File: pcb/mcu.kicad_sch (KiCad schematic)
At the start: 35 parts, among them J1 XF2M-1415-1A, SW1 EVQ-Q2B02W, SW2 EVQ-Q2B02W, U1 ESP32-S3-WROOM-1-N8R2

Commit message: Clean up and consistency
Moved buzzer to MCU
Fixed model directory
Set font size
Set outline size
Upscaled Roxy ❤️
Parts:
- added C10: 1uF, CRGM Passive:C_0603_1608Metric, symbol Device:C
- added D2: D_Schottky, CRGM Passive:D_SOD-523, symbol Device:D_Schottky
- added LS1: FUET-5025, CRG Makes:FUET-5025, symbol CRG Makes:CMT-0502-75-SMT-TR
- added Q1: MMBT2222A, CRGM Passive:SOT-523, symbol Transistor_BJT:MMBT2222A
- added R12: 1K, CRGM Passive:R_0603_1608Metric, symbol Device:R_US
- added TP42: ~, CRGM Mechanical:TestPoint_Pad_D1.0mm, symbol Connector:TestPoint
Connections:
- net +3.3V: now also C10.1, D2.1 (K), LS1.2 (+)
- net BUZZER: now also R12.1, TP42.1
- net GND: now also C10.2, Q1.2 (E)
- new net: Q1.1 (B), R12.2
- new net BUZZ_GND: D2.2 (A), LS1.3 (-), Q1.3 (C)
- no-connect marks 5 -> 6
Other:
- note added: "Buzzer"
- note added: "On Board LED"
- note removed: "ON BOARD LED"
- moved on the sheet: C7, D1, J1, TP13, TP14, TP15, TP16, TP17, TP18, TP19, TP20, TP21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

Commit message: Updated part attributes for consistency.
Updated requirements section to be more accurate.
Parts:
- C1, C10, C2, C4, C5, C7: Tolerance (none) -> 10%
- R1, R12, R2, R3: Tolerance (none) -> 5%
- U1: MN (none) -> Espressif; MPN (none) -> ESP32-S3-WROOM-1-N8R2
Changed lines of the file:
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@@
 			)
 		)
+		(property "Tolerance" "5%"
+			(at 81.28 109.22 0)
+			(effects
+				(font
+					(size 1.27 1.27)
+				)
+				(hide yes)
+			)
+		)
 		(pin "2"
 		)
@@
 			)
 		)
+		(property "Tolerance" "10%"
+			(at 39.37 162.56 0)
+			(effects
+				(font
+					(size 1.27 1.27)
+				)
+				(hide yes)
+			)
+		)
 		(pin "2"
 		)
@@
 			)
 		)
+		(property "Tolerance" "5%"
+			(at 157.48 102.87 90)
+			(effects
+				(font
+					(size 1.27 1.27)
+				)
+				(hide yes)
+			)
+		)
 		(pin "2"
 		)
@@
 			)
 		)
+		(property "Tolerance" "5%"
+			(at 90.17 109.22 0)
+			(effects
+				(font
+					(size 1.27 1.27)
+				)
+				(hide yes)
+			)
+		)
 		(pin "2"
 		)
@@
 			)
 		)
+		(property "Tolerance" "5%"
+			(at 30.48 144.78 0)
+			(effects
+				(font
+					(size 1.27 1.27)
+				)
+				(hide yes)
+			)
+		)
 		(pin "2"
 		)
@@
 			)
 		)
+		(property "Tolerance" "10%"
+			(at 123.19 114.3 0)
+			(effects
+				(font
+					(size 1.27 1.27)
+				)
+				(hide yes)
+			)
+		)
 		(pin "2"
 		)
@@
 			)
 		)
+		(property "Tolerance" "10%"
+			(at 87.63 161.29 0)
+			(effects
+				(font
+					(size 1.27 1.27)
+				)
+				(hide yes)
+			)
+		)
 		(pin "1"
 		)
@@
 			)
 		)
+		(property "Tolerance" "10%"
+			(at 198.12 109.22 0)
+			(effects
+				(font
+					(size 1.27 1.27)
+				)
+				(hide yes)
+			)
+		)
 		(pin "1"
 		)
@@
 			)
 		)
+		(property "Tolerance" "10%"
+			(at 111.76 114.3 0)
+			(effects
+				(font
+					(size 1.27 1.27)
+				)
+				(hide yes)
+			)
+		)
 		(pin "1"
 		)
@@
 			)
 		)
+		(property "MN" "Espressif"
+			(at 73.66 58.42 0)
+			(effects
+				(font
+					(size 1.27 1.27)
+				)
+				(hide yes)
+			)
+		)
+		(property "MPN" "ESP32-S3-WROOM-1-N8R2"
+			(at 73.66 58.42 0)
+			(effects
+				(font
+					(size 1.27 1.27)
+				)
+				(hide yes)
+			)
+		)
 		(pin "5"
 		)
@@
 			(at 251.46 109.22 0)
 			(effects
+				(font
+					(size 1.27 1.27)
+				)
+				(hide yes)
+			)
+		)
+		(property "Tolerance" "10%"
+			(at 251.46 109.22 0)
+			(effects

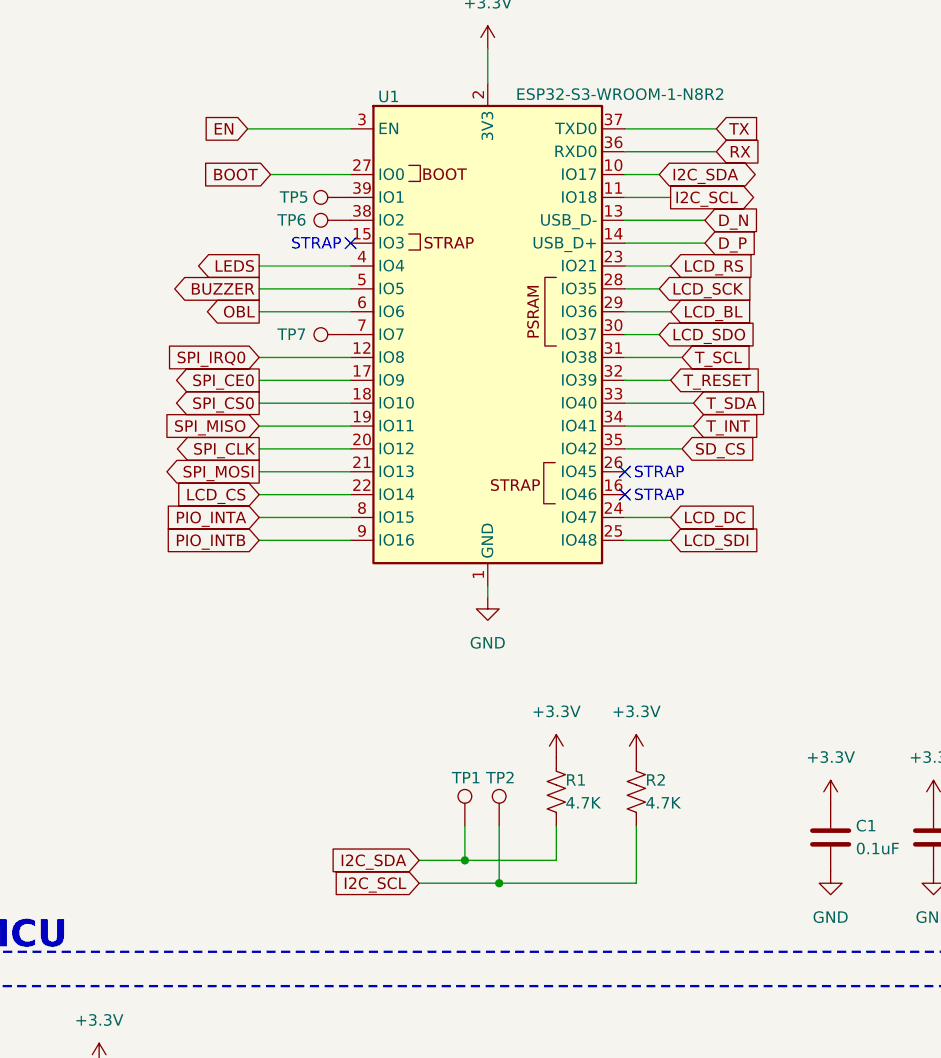
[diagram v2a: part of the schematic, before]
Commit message: Switched to internal and external I2C bus
Updated renders
Updated description of QWICC connectors
Added test points for INT I2C
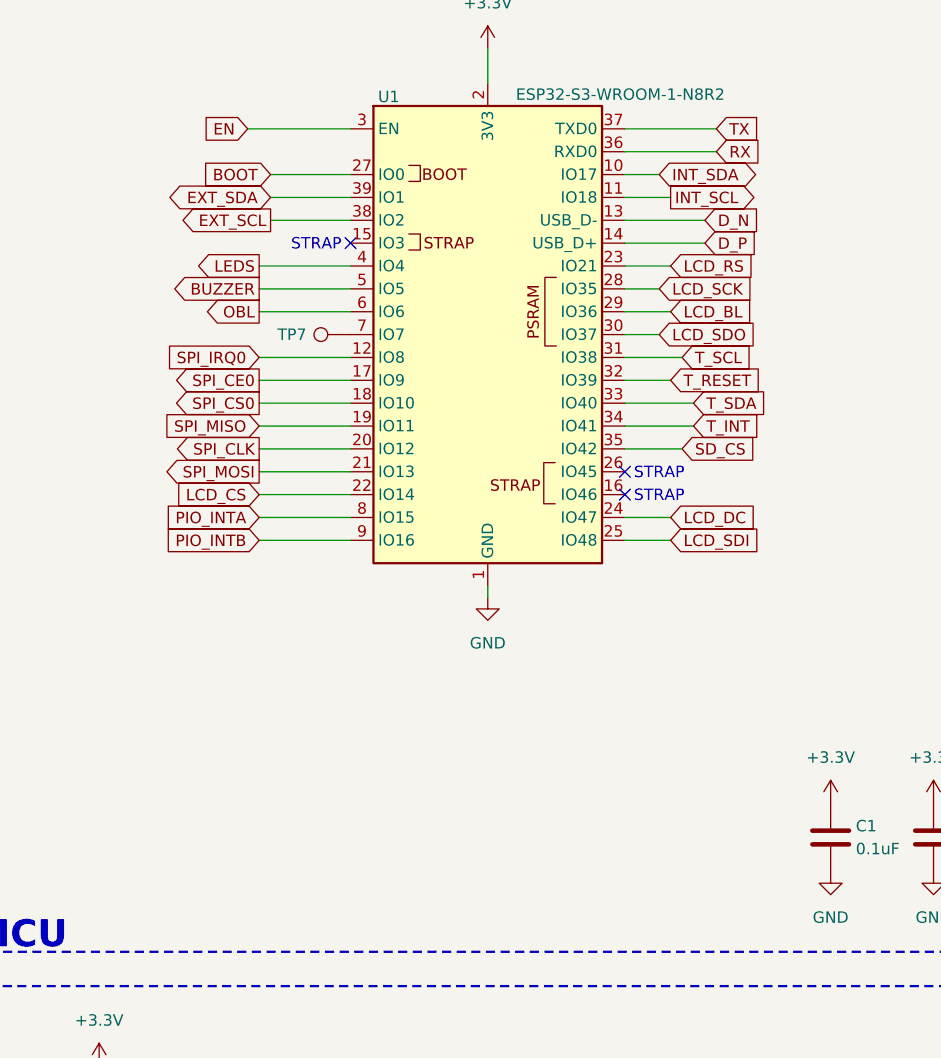
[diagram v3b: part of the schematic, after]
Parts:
- removed R1, R2: 4.7K, CRGM Passive:R_0603_1608Metric, symbol Device:R_US
- removed TP1, TP2, TP5, TP6: ~, CRGM Mechanical:TestPoint_Pad_D1.0mm, symbol Connector:TestPoint
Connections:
- net EXT_SDA: now reaches U1.39 (IO1)
- net EXT_SCL: now reaches U1.38 (IO2)
- net I2C_SCL renamed INT_SCL
- net I2C_SDA renamed INT_SDA

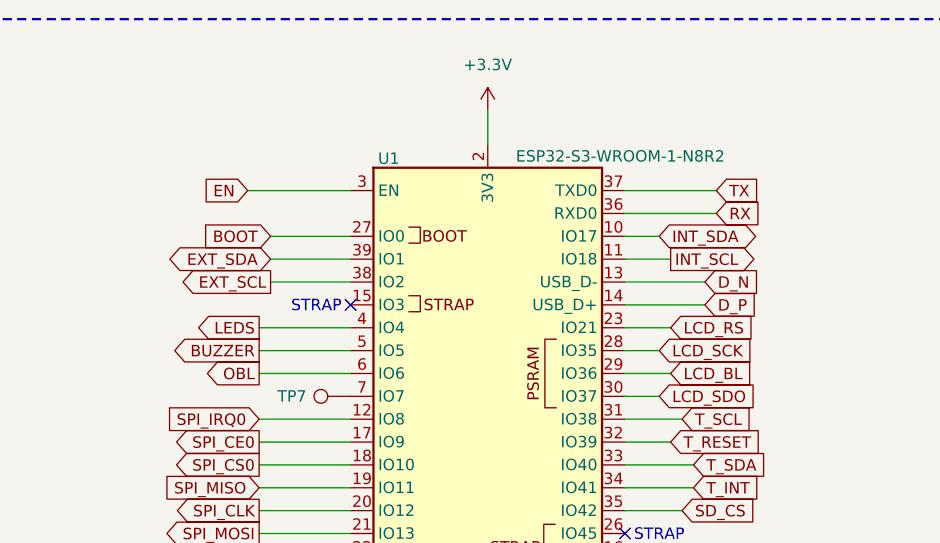
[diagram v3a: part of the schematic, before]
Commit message: Rework to add power connector
Simplified GPIO connectors to make sure for power.
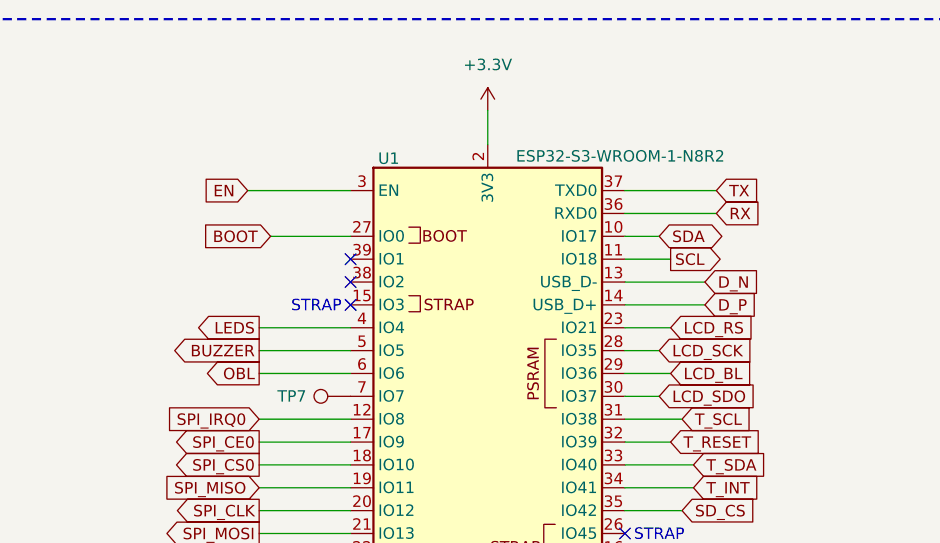
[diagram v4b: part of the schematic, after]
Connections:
- net EXT_SCL: no longer names the net of U1.38 (IO2)
- net EXT_SDA: no longer names the net of U1.39 (IO1)
- net INT_SCL renamed SCL
- net INT_SDA renamed SDA
- no-connect marks 6 -> 8
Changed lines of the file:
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@@
 	)
 	(no_connect
+		(at 58.42 45.72)
+	)
+	(no_connect
 		(at 171.45 87.63)
 	)
 	(no_connect
+		(at 58.42 43.18)
+	)
+	(no_connect
 		(at 223.52 59.69)
 	)
@@
 	(wire
 		(pts
-			(xy 49.53 43.18) (xy 58.42 43.18)
-		)
-		(stroke
-			(width 0)
-			(type default)
-		)
-	)
-	(wire
-		(pts
 			(xy 96.52 152.4) (xy 99.06 152.4)
 		)
@@
 	(wire
 		(pts
-			(xy 49.53 45.72) (xy 58.42 45.72)
-		)
-		(stroke
-			(width 0)
-			(type default)
-		)
-	)
-	(wire
-		(pts
 			(xy 30.48 152.4) (xy 30.48 158.75)
 		)
@@
 		)
 	)
-	(global_label "EXT_SDA"
-		(shape bidirectional)
-		(at 49.53 43.18 180)
-		(fields_autoplaced yes)
-		(effects
-			(font
-				(size 1.27 1.27)
-			)
-			(justify right)
-		)
-		(property "Intersheetrefs" "${INTERSHEET_REFS}"
-			(at 37.5717 43.18 0)
-			(effects
-				(font
-					(size 1.27 1.27)
-				)
-				(justify right)
-			)
-		)
-	)
 	(global_label "SPI_IRQ0"
 		(shape input)
@@
 		)
 	)
-	(global_label "EXT_SCL"
-		(shape output)
-		(at 49.53 45.72 180)
-		(fields_autoplaced yes)
-		(effects
-			(font
-				(size 1.27 1.27)
-			)
-			(justify right)
-		)
-		(property "Intersheetrefs" "${INTERSHEET_REFS}"
-			(at 38.7435 45.72 0)
-			(effects
-				(font
-					(size 1.27 1.27)
-				)
-				(justify right)
-			)
-		)
-	)
 	(global_label "SD_CS"
 		(shape input)
@@
 		)
 	)
-	(global_label "INT_SCL"
+	(global_label "SCL"
 		(shape output)
 		(at 93.98 43.18 0)
@@
 		)
 		(property "Intersheetrefs" "${INTERSHEET_REFS}"
-			(at 104.3433 43.18 0)
+			(at 100.4728 43.18 0)
 			(effects
 				(font
@@
 		)
 	)
-	(global_label "INT_SDA"
+	(global_label "SDA"
 		(shape bidirectional)
 		(at 92.71 40.64 0)
@@
 		)
 		(property "Intersheetrefs" "${INTERSHEET_REFS}"
-			(at 104.2451 40.64 0)
+			(at 100.3746 40.64 0)
 			(effects
 				(font

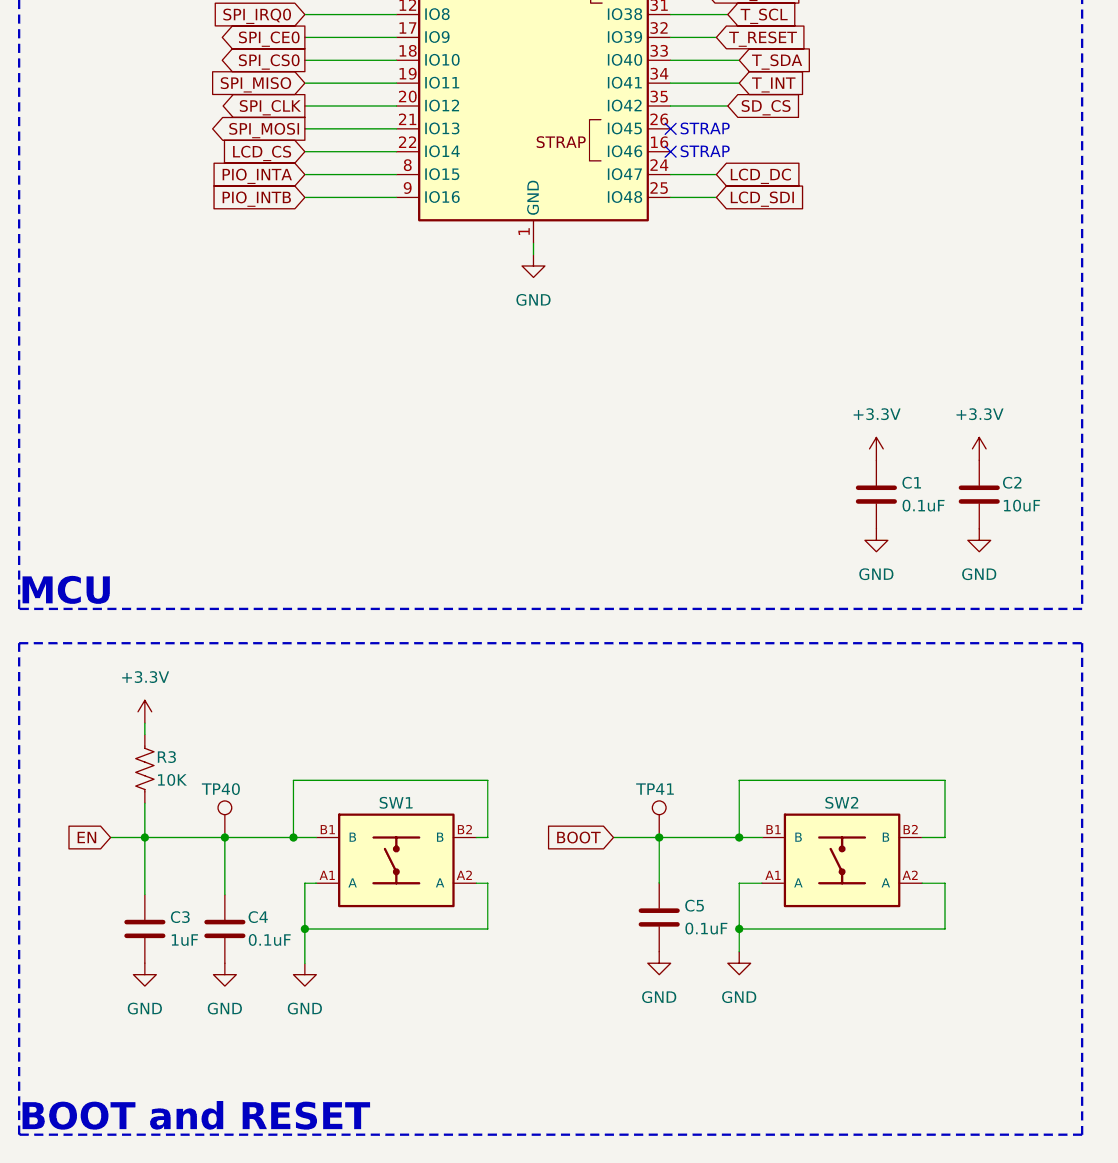
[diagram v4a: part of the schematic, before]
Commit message: Moved connectors
Moved I2C to edge
Rearranged all GPIO
Re-routed as necessary
(I don't like the button connector layout -- like the old way more)
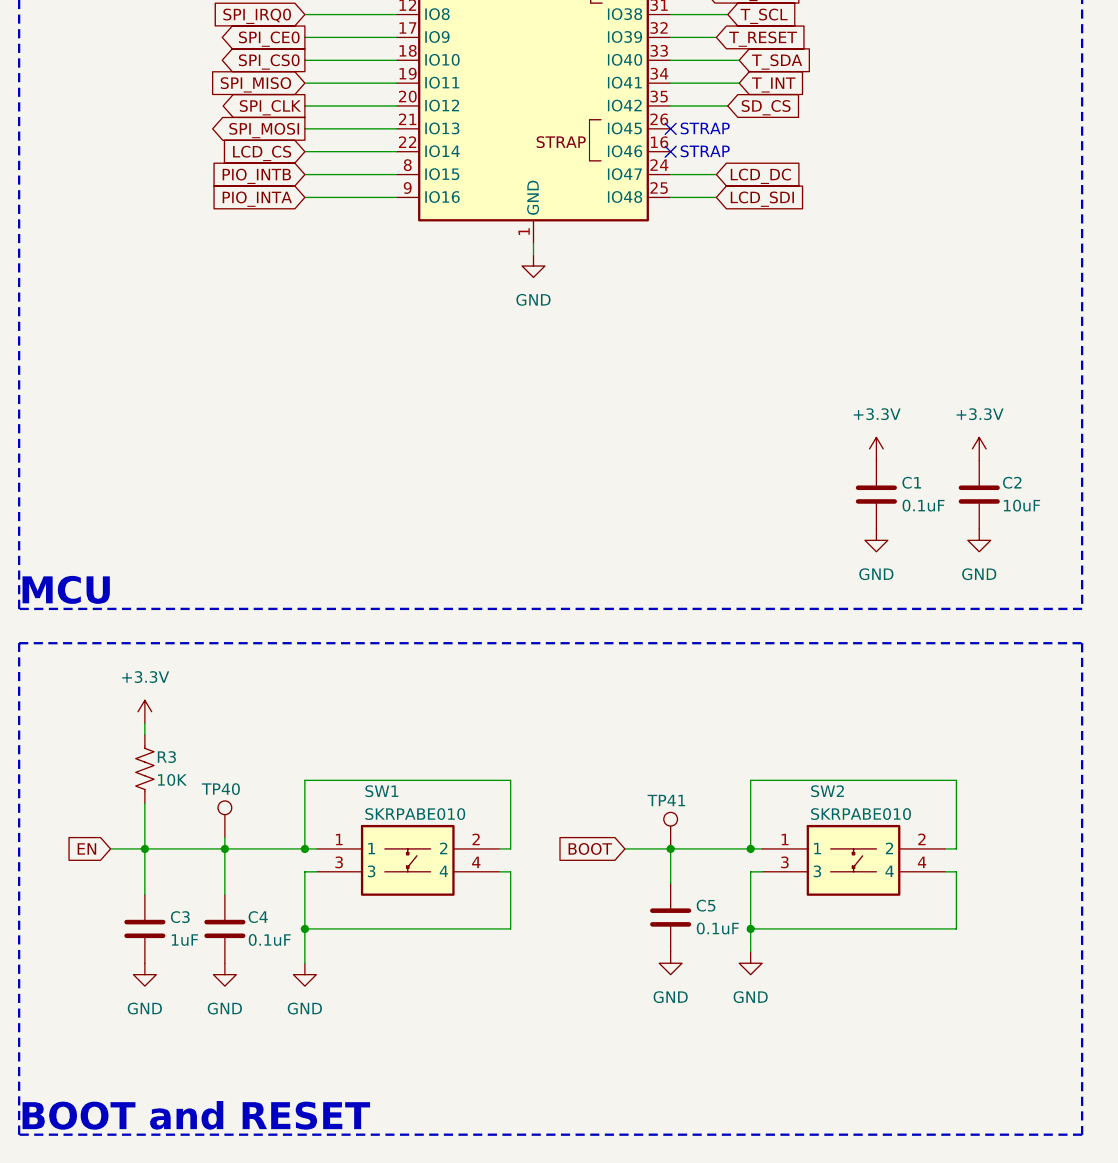
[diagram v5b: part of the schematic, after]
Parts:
- removed SW1, SW2: EVQ-Q2B02W, CRGM Switches:EVQ-Q2B02W, symbol CRGM Switches:EVQ-Q2B02W
- added SW1, SW2: SKRPABE010, CRGM Switches:SMD-4P-4.2x3.2mm, symbol CRGM Switches:SKRPABE010
- C10, C3: MPN CGA0603X5R105K160JT -> CL10B105KO8NNNC
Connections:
- net BOOT: now also SW2.1, SW2.2
- net EN: now also SW1.1, SW1.2
- net GND: now also SW1.3, SW1.4, SW2.3, SW2.4
- net PIO_INTA: now also U1.9 (IO16); no longer U1.8 (IO15)
- net PIO_INTB: now also U1.8 (IO15); no longer U1.9 (IO16)
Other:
- moved on the sheet: C5, TP41

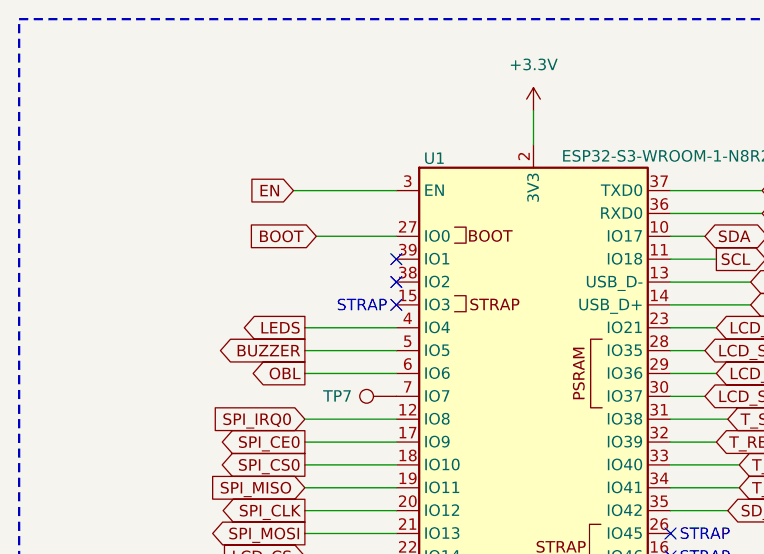
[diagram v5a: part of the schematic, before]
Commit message: Fixed GPIO resistor annoyance
Better ground now
Stitching vias all around
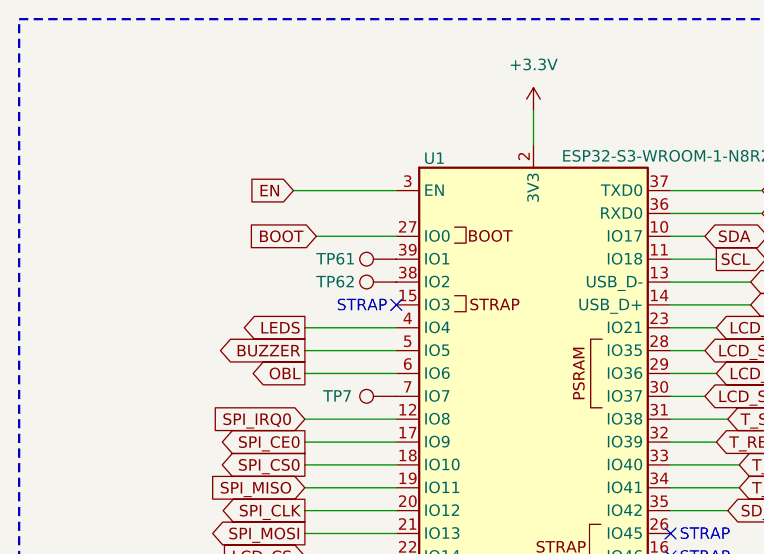
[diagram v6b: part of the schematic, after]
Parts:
- added TP61, TP62: ~, CRGM Mechanical:TestPoint_Pad_D1.0mm, symbol Connector:TestPoint
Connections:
- net at U1.38 (IO2): now also TP62.1
- net at U1.39 (IO1): now also TP61.1
- no-connect marks 8 -> 6
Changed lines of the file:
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@@
 	)
 	(no_connect
-		(at 58.42 45.72)
-	)
-	(no_connect
 		(at 171.45 87.63)
 	)
 	(no_connect
-		(at 58.42 43.18)
-	)
-	(no_connect
 		(at 223.52 59.69)
 	)
@@
 	)
 	(symbol
+		(lib_id "Connector:TestPoint")
+		(at 58.42 45.72 90)
+		(unit 1)
+		(exclude_from_sim no)
+		(in_bom no)
+		(on_board yes)
+		(dnp no)
+		(property "Reference" "TP62"
+			(at 49.53 45.72 90)
+			(effects
+				(font
+					(size 1.27 1.27)
+				)
+				(justify right)
+			)
+		)
+		(property "Value" "~"
+			(at 46.99 45.72 90)
+			(effects
+				(font
+					(size 1.27 1.27)
+				)
+				(justify right)
+				(hide yes)
+			)
+		)
+		(property "Footprint" "CRGM Mechanical:TestPoint_Pad_D1.0mm"
+			(at 58.42 40.64 0)
+			(effects
+				(font
+					(size 1.27 1.27)
+				)
+				(hide yes)
+			)
+		)
+		(property "Datasheet" "~"
+			(at 58.42 40.64 0)
+			(effects
+				(font
+					(size 1.27 1.27)
+				)
+				(hide yes)
+			)
+		)
+		(property "Description" "test point"
+			(at 58.42 45.72 0)
+			(effects
+				(font
+					(size 1.27 1.27)
+				)
+				(hide yes)
+			)
+		)
+		(pin "1"
+		)
+		(instances
+			(project "aquarius-hub-hw"
+				(path "/39407804-2746-45a9-a901-1039a9921518/2500e019-c938-4e9e-9faa-9174484e036e"
+					(reference "TP62")
+					(unit 1)
+				)
+			)
+		)
+	)
+	(symbol
 		(lib_id "power:+3.3V")
 		(at 198.12 104.14 0)
@@
 					(unit 1)
 				)
+			)
+		)
+	)
+	(symbol
+		(lib_id "Connector:TestPoint")
+		(at 58.42 43.18 90)
+		(unit 1)
+		(exclude_from_sim no)
+		(in_bom no)
+		(on_board yes)
+		(dnp no)
+		(property "Reference" "TP61"
+			(at 49.53 43.18 90)
+			(effects
+				(font
+					(size 1.27 1.27)
+				)
+				(justify right)
+			)
+		)
+		(property "Value" "~"
+			(at 46.99 43.18 90)
+			(effects
+				(font
+					(size 1.27 1.27)
+				)
+				(justify right)
+				(hide yes)
+			)
+		)
+		(property "Footprint" "CRGM Mechanical:TestPoint_Pad_D1.0mm"
+			(at 58.42 38.1 0)
+			(effects
+				(font
+					(size 1.27 1.27)
+				)
+				(hide yes)
+			)
+		)
+		(property "Datasheet" "~"
+			(at 58.42 38.1 0)
+			(effects
+				(font
+					(size 1.27 1.27)
+				)
+				(hide yes)
+			)
+		)
+		(property "Description" "test point"
+			(at 58.42 43.18 0)
+			(effects
+				(font
+					(size 1.27 1.27)
+				)
+				(hide yes)
+			)
+		)
+		(pin "1"
+		)
+		(instances
+			(project "aquarius-hub-hw"
+				(path "/39407804-2746-45a9-a901-1039a9921518/2500e019-c938-4e9e-9faa-9174484e036e"
+					(reference "TP61")
+					(unit 1)
+				)
